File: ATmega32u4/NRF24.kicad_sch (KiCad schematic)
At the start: 1 part, among them J3 NRF24

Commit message: Schematic, routing and layout changes post review.
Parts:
- J3: now in the parts list
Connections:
- net CE renamed PE6-CE
- net CSN renamed PB4-CSN
- net IRQ renamed PF1-IRQ
- net MISO renamed PB3-MISO
- net MOSI renamed PB2-MOSI
- net SCK renamed PB1-SCK
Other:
- note added: "Notes: Essentially just an SPI bus to 2.54mm headers"
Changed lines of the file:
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@@
     (stroke (width 0) (type default) (color 0 0 0 0))
   )
-  (label "IRQ" (at 132.08 85.09 0)
+  (text "Notes:\n\nEssentially just an SPI bus to 2.54mm headers"
+    (at 12.7 196.85 0)
     (effects (font (size 1.27 1.27)) (justify left bottom))
   )
-  (label "MOSI" (at 132.08 87.63 0)
+  (label "PF1-IRQ" (at 132.08 85.09 0)
     (effects (font (size 1.27 1.27)) (justify left bottom))
   )
-  (label "MISO" (at 132.08 67.31 0)
+  (label "PB2-MOSI" (at 132.08 87.63 0)
     (effects (font (size 1.27 1.27)) (justify left bottom))
   )
-  (label "CE" (at 132.08 62.23 0)
+  (label "PB3-MISO" (at 132.08 67.31 0)
     (effects (font (size 1.27 1.27)) (justify left bottom))
   )
-  (label "SCK" (at 132.08 64.77 0)
+  (label "PE6-CE" (at 132.08 62.23 0)
     (effects (font (size 1.27 1.27)) (justify left bottom))
   )
-  (label "CSN" (at 132.08 90.17 0)
+  (label "PB1-SCK" (at 132.08 64.77 0)
+    (effects (font (size 1.27 1.27)) (justify left bottom))
+  )
+  (label "PB4-CSN" (at 132.08 90.17 0)
     (effects (font (size 1.27 1.27)) (justify left bottom))
   )
@@
   )
   (symbol (lib_id "Connector_Generic:Conn_02x04_Odd_Even") (at 156.21 74.93 270) (unit 1)
-    (in_bom no) (on_board yes)
+    (in_bom yes) (on_board yes)
     (property "Reference" "J3" (id 0) (at 161.29 76.2 90)
       (effects (font (size 1.27 1.27)) (justify left))

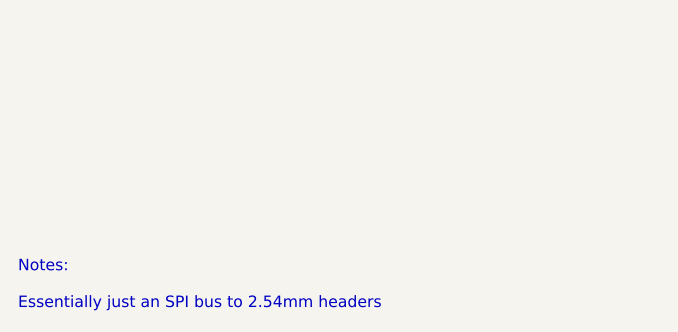
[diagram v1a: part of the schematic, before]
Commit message: Update notes, add io for reading cc pins, minor changes to schematic and routing.
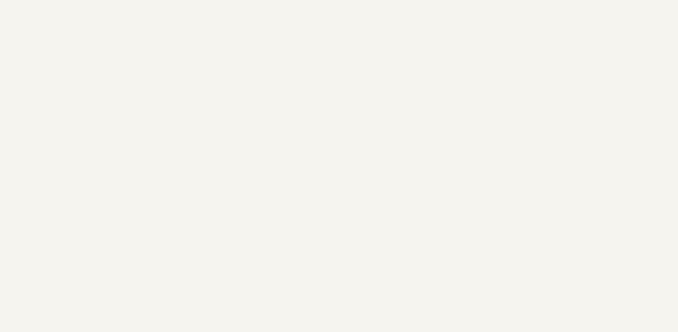
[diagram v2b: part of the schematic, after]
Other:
- note removed: "Notes: Essentially just an SPI bus to 2.54mm headers"
- title: (none) -> OpenRetroPad
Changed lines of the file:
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@@
 (kicad_sch (version 20211123) (generator eeschema)
   (paper "A4")
+  (title_block
+    (title "OpenRetroPad")
+    (date "2022-12-29")
+    (rev "2")
+    (comment 3 "github.com/OpenRetroPad")
+    (comment 4 "ATmega32u4")
+  )
   (bus_entry (at 129.54 87.63) (size 2.54 2.54)
     (stroke (width 0) (type default) (color 0 0 0 0))
@@
     (stroke (width 0) (type default) (color 0 0 0 0))
   )
-  (text "Notes:\n\nEssentially just an SPI bus to 2.54mm headers"
-    (at 12.7 196.85 0)
-    (effects (font (size 1.27 1.27)) (justify left bottom))
-  )
   (label "PF1-IRQ" (at 132.08 85.09 0)
